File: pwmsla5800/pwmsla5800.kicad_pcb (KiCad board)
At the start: 2 copper layers, 63.5 x 76.2 mm, 30 parts, among them Q1 BC547, Q2 BC547, U1 LM324

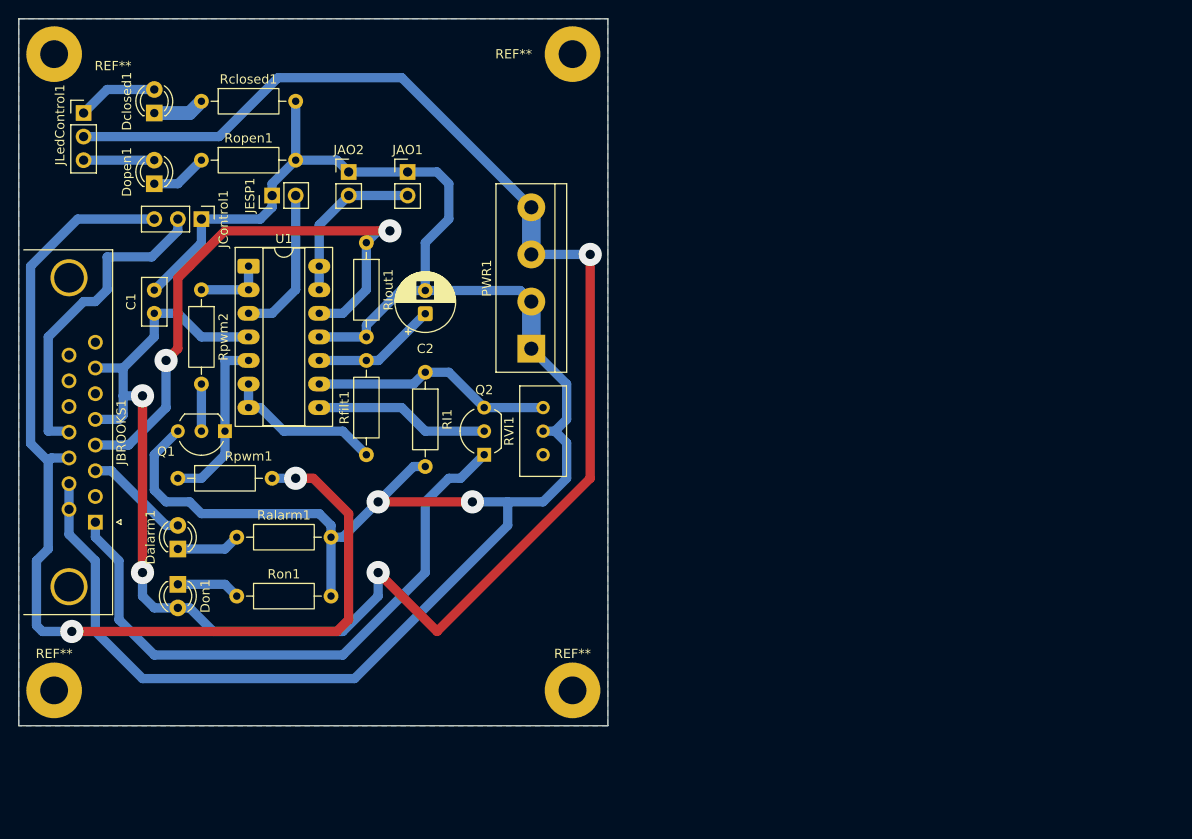
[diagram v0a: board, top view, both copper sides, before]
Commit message: New concept. Generating the 4-20mA current is done on an outside module
Until I figure out how generate the current well, I think it is better just use a Chinese board.

When generating the PWM, to obtain a stable voltage I am using a TL431 circuit.
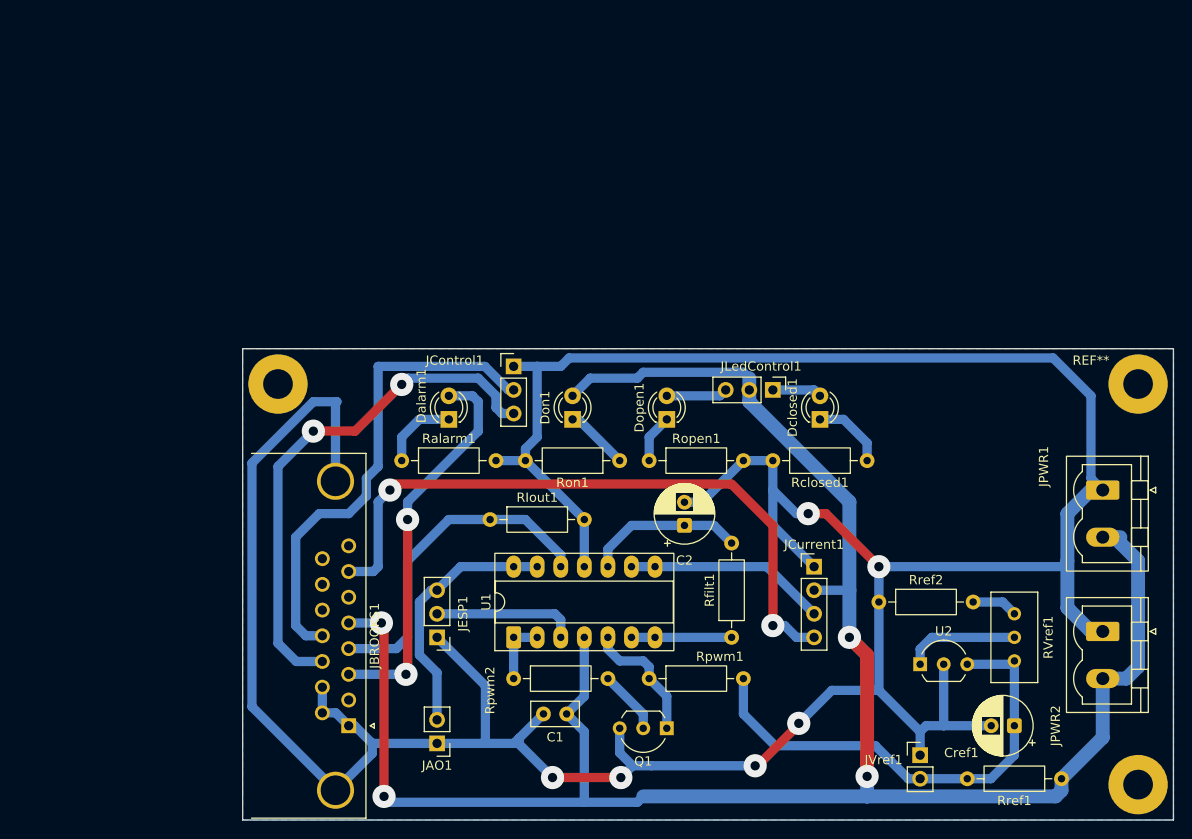
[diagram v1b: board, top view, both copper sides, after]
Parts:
- removed JAO2: Conn_01x02, Connector_PinHeader_2.54mm:PinHeader_1x02_P2.54mm_Vertical
- removed PWR1: Conn_01x04, TerminalBlock:TerminalBlock_bornier-4_P5.08mm
- removed Q2: BC547, Package_TO_SOT_THT:TO-92_Inline_Wide
- removed the REF** at (67.3, 123.2)
- removed the REF** at (123.2, 54.6)
- removed the REF** at (123.2, 123.2)
- removed the REF** at (67.3, 54.6)
- removed RI1: 250, Resistor_THT:R_Axial_DIN0207_L6.3mm_D2.5mm_P10.16mm_Horizontal
- removed RVI1: 1k, Potentiometer_THT:Potentiometer_Bourns_3296W_Vertical
- added ?: , , F.Cu at (184.2, 133.3)
- added ?: , , F.Cu at (91.4, 90.2)
- added Cref1: 10u, Capacitor_THT:CP_Radial_D6.3mm_P2.50mm, F.Cu at (170.8, 127.0)
- added JCurrent1: Conn_01x04, Connector_PinHeader_2.54mm:PinHeader_1x04_P2.54mm_Vertical, F.Cu at (149.2, 109.9)
- added JPWR1: Conn_01x02, Connector_Phoenix_MSTB:PhoenixContact_MSTBVA_2,5_2-G-5,08_1x02_P5.08mm_Vertical, F.Cu at (180.3, 101.6)
- added JPWR2: Conn_01x02, Connector_Phoenix_MSTB:PhoenixContact_MSTBVA_2,5_2-G-5,08_1x02_P5.08mm_Vertical, F.Cu at (180.3, 116.8)
- added JVref1: Conn_01x02, Connector_PinHeader_2.54mm:PinHeader_1x02_P2.54mm_Vertical, F.Cu at (160.7, 130.2)
- added REF**: Hole, MountingHole:MountingHole_3.2mm_M3_Pad, F.Cu at (184.2, 90.2)
- added RVref1: 10k, Potentiometer_THT:Potentiometer_Bourns_3296W_Vertical, F.Cu at (170.8, 120.0)
- added Rref1: 2k, Resistor_THT:R_Axial_DIN0207_L6.3mm_D2.5mm_P10.16mm_Horizontal, F.Cu at (175.9, 132.7)
- added Rref2: 1k, Resistor_THT:R_Axial_DIN0207_L6.3mm_D2.5mm_P10.16mm_Horizontal, F.Cu at (156.2, 113.7)
- added U2: TL431LP, Package_TO_SOT_THT:TO-92_Inline_Wide, F.Cu at (160.7, 120.4)
- C2: value C_Polarized -> 10u
- JBROOKS1: value Conn_01x15 -> DA15_Socket_MountingHoles; footprint Connector_Dsub:DSUB-15_Socket_Horizontal_P2.77x2.84mm_EdgePinOffset4.94mm_Housed_MountingHolesOffset4.94mm -> Connector_Dsub:DSUB-15_Socket_Horizontal_P2.77x2.84mm_EdgePinOffset7.70mm_Housed_MountingHolesOffset9.12mm
- JESP1: value Conn_01x02 -> Conn_01x03; footprint Connector_PinHeader_2.54mm:PinHeader_1x02_P2.54mm_Vertical -> Connector_PinHeader_2.54mm:PinHeader_1x03_P2.54mm_Vertical
- moved Rclosed1 81.5 mm to (154.9, 98.4), turned to 180 degrees
- moved JLedControl1 80.1 mm to (144.8, 90.8), turned to -90 degrees
- moved Dclosed1 79.0 mm to (149.9, 94.0)
- moved C1 62.0 mm to (122.6, 125.7), turned to 180 degrees
- moved JAO1 61.7 mm to (108.6, 128.9), turned to 180 degrees
- moved Dopen1 60.8 mm to (133.3, 94.0)
- moved Ropen1 58.1 mm to (131.4, 98.4)
- moved Q1 57.4 mm to (133.3, 127.3)
- moved Rpwm1 55.2 mm to (131.4, 121.9)
- moved Rpwm2 53.8 mm to (116.8, 121.9), turned to 0 degrees
- moved JESP1 50.8 mm to (108.6, 117.5), turned to 180 degrees
- moved U1 49.2 mm to (116.8, 117.5), turned to 90 degrees
- moved Don1 46.1 mm to (123.2, 94.0), turned to 90 degrees
- moved Rfilt1 44.0 mm to (140.3, 117.5)
- moved Ron1 43.8 mm to (128.3, 98.4), turned to 180 degrees
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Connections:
- JBROOKS1 pad 0: (no net) -> GND
- JBROOKS1 pad 1: /Iinput -> GND
- JBROOKS1 pad 7: +24V -> /Iinput
- Rpwm1 pad 2: +5V -> /Vref
- U1 pad 8: Net-(Q2-B) -> /Vinput
- U1 pad 9: Net-(Q2-E) -> /Vinput
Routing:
- net GND: track 253.1 -> 378.2 mm, vias 2 -> 6
- net +5V: track 113.6 -> 56.4 mm
- net /Vref: track 0.00 -> 52.4 mm
- net /Alarm: track 11.3 -> 42.5 mm, vias 0 -> 2
- net /AO: track 63.0 -> 36.3 mm, vias 2 -> 0
- net Net-(Q2-E): track 26.2 -> 0.00 mm
- net /Vinput: track 0.00 -> 21.8 mm
- net Net-(Q2-B): track 18.8 -> 0.00 mm
- net /Vcontrol: track 34.5 -> 52.5 mm
- net +24V: track 209.1 -> 226.9 mm
- net Net-(U2-REF): track 0.00 -> 12.3 mm
- net /Vout: track 17.8 -> 27.8 mm
- net Net-(U1B--): track 17.3 -> 10.8 mm
- net /Iinput: track 65.9 -> 71.3 mm, vias 0 -> 2
- net Net-(RVref1-Pad3): track 0.00 -> 4.97 mm
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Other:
- board size 63.5 x 76.2 mm -> 100.3 x 50.8 mm

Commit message: Corrected small bug in `pwm_mwtt.cpp` and updated R values in the board.
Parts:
- Ralarm1, Rclosed1, Ron1, Ropen1: value R -> 1.5k
- Rref2: value 1k -> 10k
